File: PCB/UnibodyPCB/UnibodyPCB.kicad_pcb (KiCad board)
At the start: 2 copper layers, 11 parts, among them J1 Conn_01x12, J2 Conn_01x12, J3 Conn_01x03

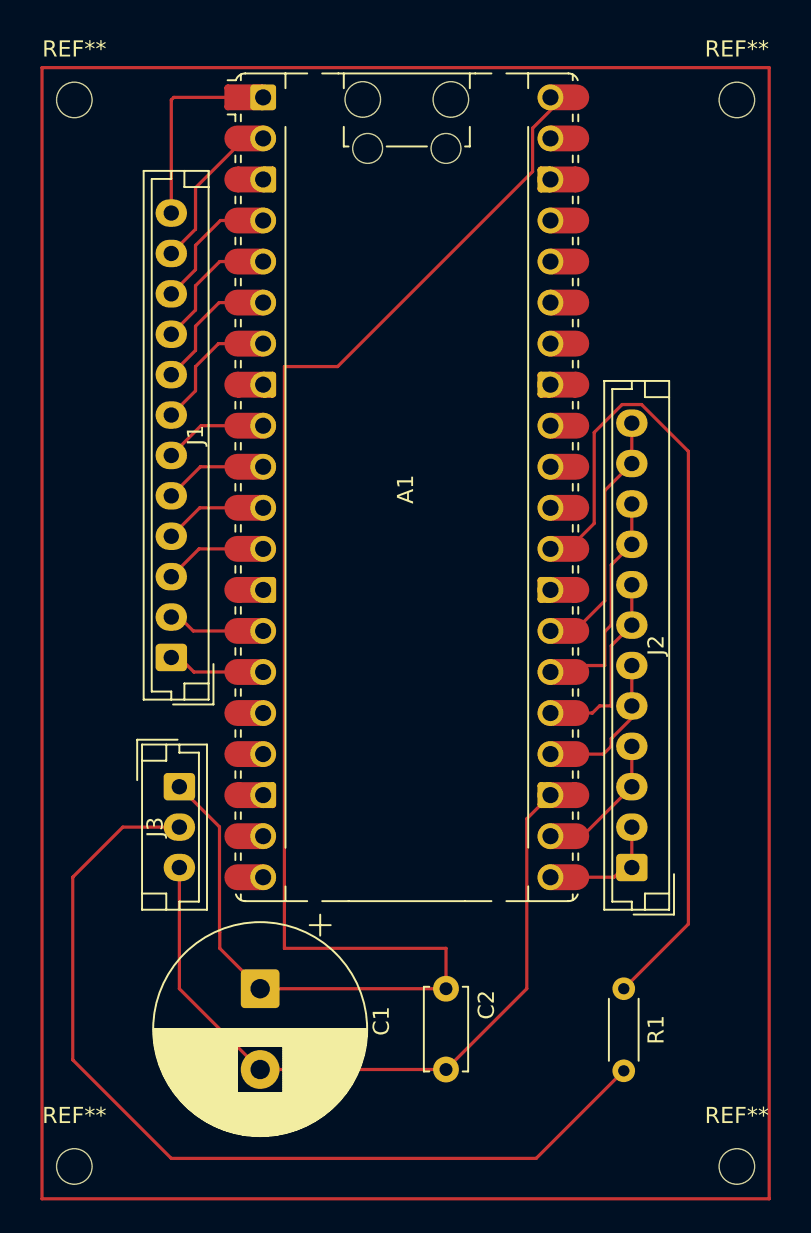
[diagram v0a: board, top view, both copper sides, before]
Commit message: Update PCB files - mounting holes moved
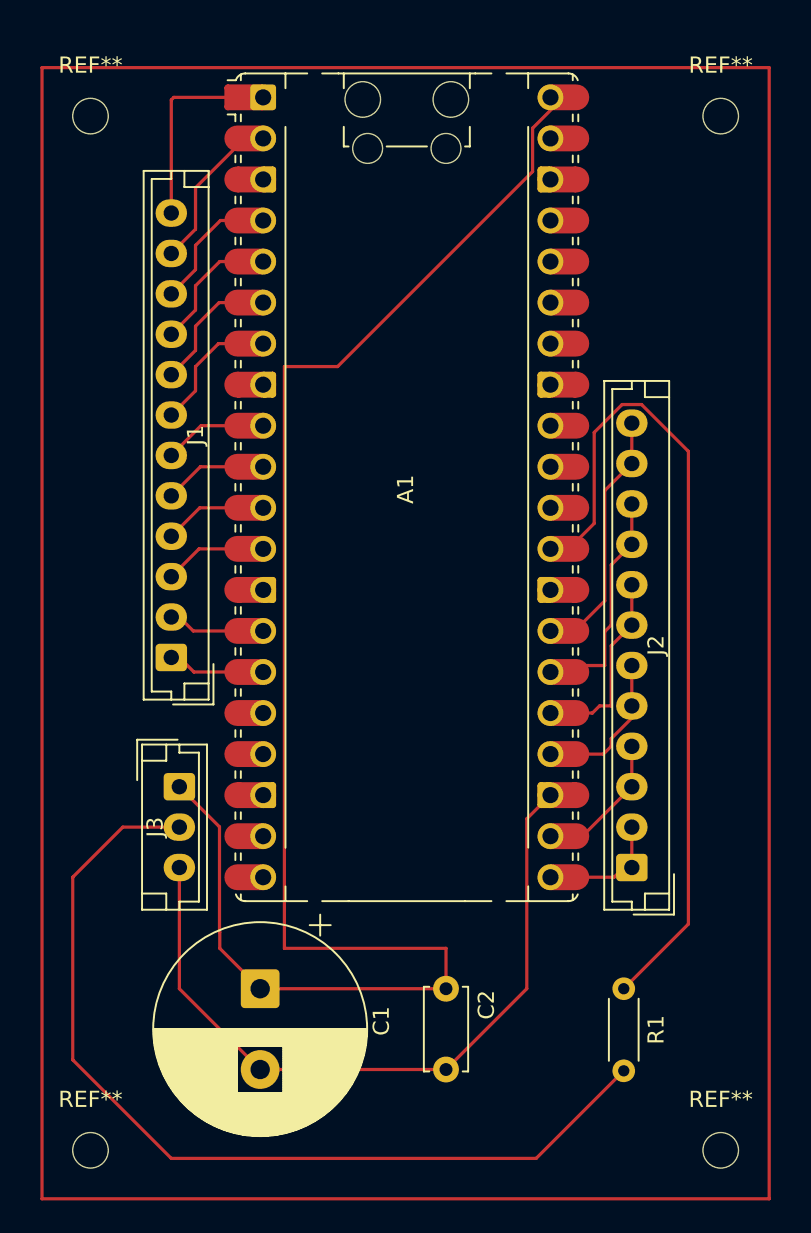
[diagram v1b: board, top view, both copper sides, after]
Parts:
- moved REF** 1.41 mm to (103.0, 117.0)
- moved REF** 1.41 mm to (142.0, 53.0)
- moved REF** 1.41 mm to (103.0, 53.0)
- moved REF** 1.41 mm to (142.0, 117.0)
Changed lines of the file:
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@@
 	(footprint "MountingHole:MountingHole_2.2mm_M2"
 		(layer "F.Cu")
-		(at 102 118)
+		(at 103 117)
 		(descr "Mounting Hole 2.2mm, M2, no annular, generated by kicad-footprint-generator mountinghole.py")
 		(tags "mountinghole M2")
@@
 	(footprint "MountingHole:MountingHole_2.2mm_M2"
 		(layer "F.Cu")
-		(at 143 52)
+		(at 142 53)
 		(descr "Mounting Hole 2.2mm, M2, no annular, generated by kicad-footprint-generator mountinghole.py")
 		(tags "mountinghole M2")
@@
 	(footprint "MountingHole:MountingHole_2.2mm_M2"
 		(layer "F.Cu")
-		(at 102 52)
+		(at 103 53)
 		(descr "Mounting Hole 2.2mm, M2, no annular, generated by kicad-footprint-generator mountinghole.py")
 		(tags "mountinghole M2")
@@
 	(footprint "MountingHole:MountingHole_2.2mm_M2"
 		(layer "F.Cu")
-		(at 143 118)
+		(at 142 117)
 		(descr "Mounting Hole 2.2mm, M2, no annular, generated by kicad-footprint-generator mountinghole.py")
 		(tags "mountinghole M2")

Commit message: Improve mounting hole for pcb
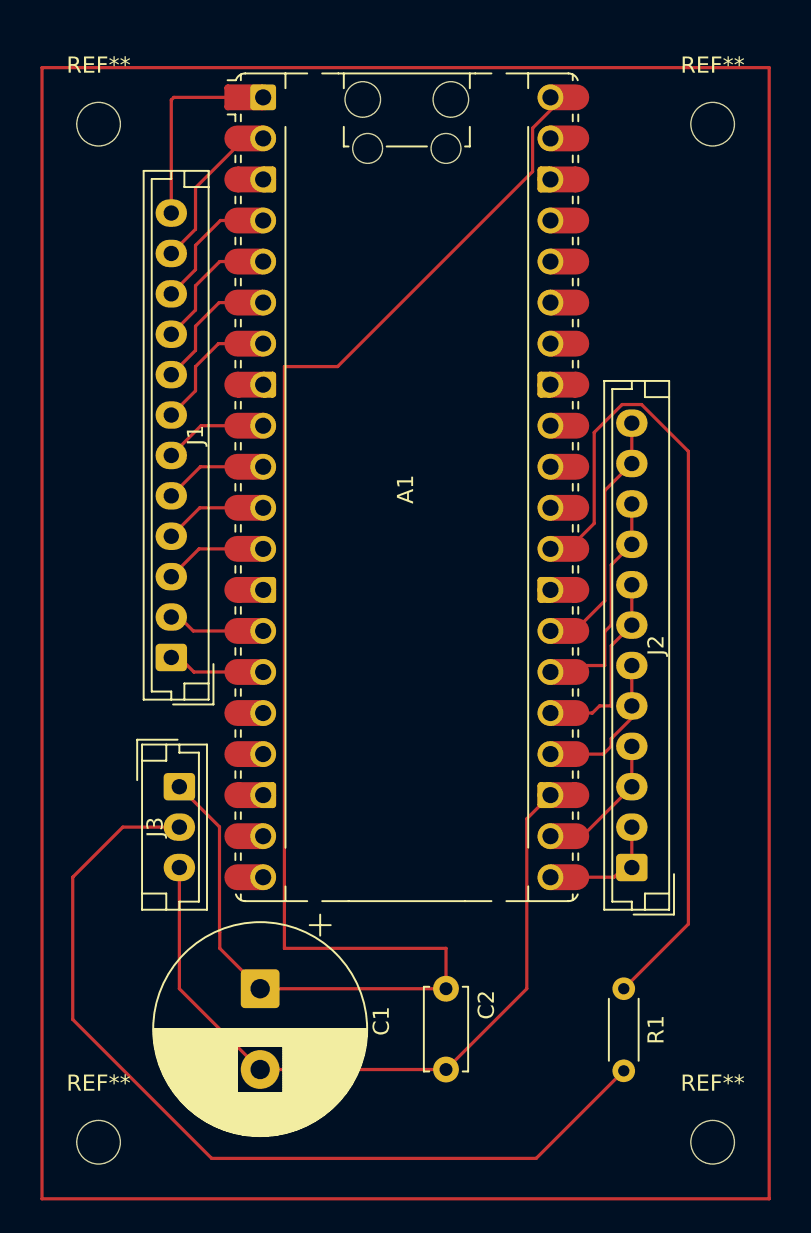
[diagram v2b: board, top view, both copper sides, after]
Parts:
- removed the REF** at (103.0, 117.0)
- removed the REF** at (142.0, 53.0)
- removed the REF** at (103.0, 53.0)
- removed the REF** at (142.0, 117.0)
- added REF**: MountingHole_2.7mm_M2.5, MountingHole:MountingHole_2.7mm_M2.5, F.Cu at (103.5, 53.5)
- added REF**: MountingHole_2.7mm_M2.5, MountingHole:MountingHole_2.7mm_M2.5, F.Cu at (141.5, 116.5)
- added REF**: MountingHole_2.7mm_M2.5, MountingHole:MountingHole_2.7mm_M2.5, F.Cu at (103.5, 116.5)
- added REF**: MountingHole_2.7mm_M2.5, MountingHole:MountingHole_2.7mm_M2.5, F.Cu at (141.5, 53.5)
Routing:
- net Net-(J3-Pin_2): track 58.1 -> 56.6 mm
